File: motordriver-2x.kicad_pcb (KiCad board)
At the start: 4 copper layers, 215 x 130 mm, 651 parts, among them J1 USB_B_Micro, J2 CONN_RJ45_MAG, J3 CONN_RJ45_MAG, P1 CONN_BUTTON, P11 CONN_JOYSTICK, P13 CONN_SENSOR, P14 CONN_SENSOR, P15 CONN_SENSOR, P16 CONN_SENSOR, P17 CONN_DEBUG_2R, P18 CONN_POWER_41A, P19 CONN_CAN, P2 CONN_BUTTON, P20 CONN_CAN, P21 CONN_AN_OUT, P22 CONN_AN_OUT, P23 CONN_POWER_10A, P24 CONN_CAN, P25 CONN_LCD, P26 CONN_AN_OUT, P27 CONN_AN_OUT, P28 CONN_UEXT, P3 CONN_BUTTON, P37 CONN_ENCODER, P38 CONN_SENSOR, P39 CONN_SENSOR, P4 CONN_BUTTON, P40 CONN_SENSOR, P41 CONN_ENCODER, P42 CONN_SENSOR, P43 CONN_SENSOR, P44 CONN_SENSOR, P45 CONN_MOTOR, P46 CONN_MOTOR, P47 CONN_HALL, P48 CONN_HALL, P49 CONN_BRKRES, P5 CONN_BUTTON, P6 CONN_BUTTON, P7 CONN_BUTTON, P8 CONN_BUTTON, P9 CONN_JOYSTICK, Q1 Q_NMOS_2X_60V_63A, Q2 Q_NMOS_2X_60V_63A, Q3 Q_NMOS_2X_60V_63A, Q4 Q_NMOS_2X_60V_63A, Q5 Q_NMOS_2X_60V_63A, Q6 Q_NMOS_2X_60V_63A, Q7 Q_PNP_BC856, Q8 Q_NMOS_BUK9875, U1 IC_MIC2026, U10 IC_MCP4461, U11 IC_MCP2517FD-xJHA, U12 IC_STM32F429ZET6, U13 IC_MCP23S17, U14 IC_TPS54360DDA, U15 IC_TJA1044GT3, U16 IC_TLV2474, U17 IC_M24C16, U18 IC_USBLC6-2, U19 IC_TPS62147RGXR, U2 IC_MAX6818, U20 IC_TLV75533, U21 IC_LP55231, U22 IC_TLV75533, U23 IC_MAX14890, U24 IC_MAX14890, U25 IC_MIC2026, U26 IC_TLV2474, U27 IC_USBLC6-2, U28 IC_USBLC6-2, U29 IC_MCP4461, U3 IC_TLV2474, U30 IC_LAN9252, U31 IC_DRV8302, U32 IC_DRV8302, U33 IC_TLV2474, U34 IC_M24C16, U35 IC_TLV2474, U36 IC_TLV75533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

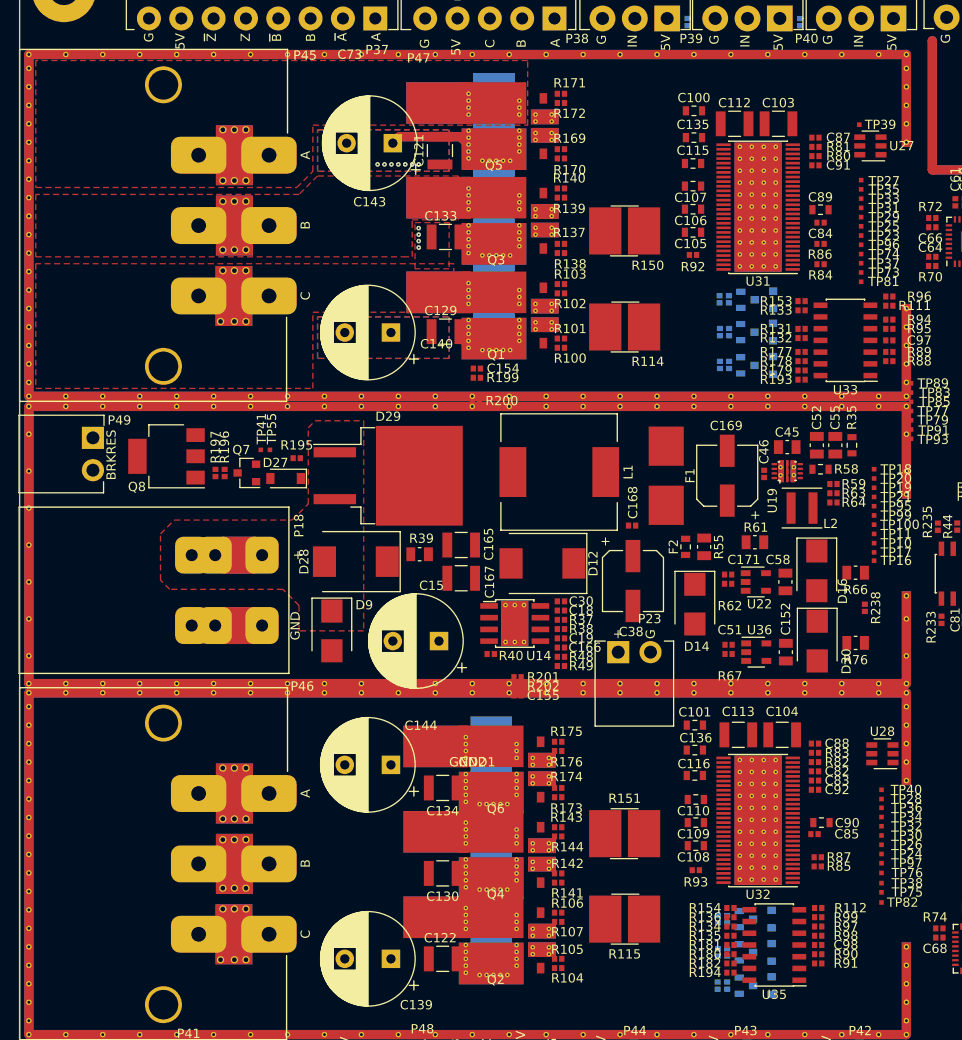
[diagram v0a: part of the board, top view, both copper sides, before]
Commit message: routing with fills
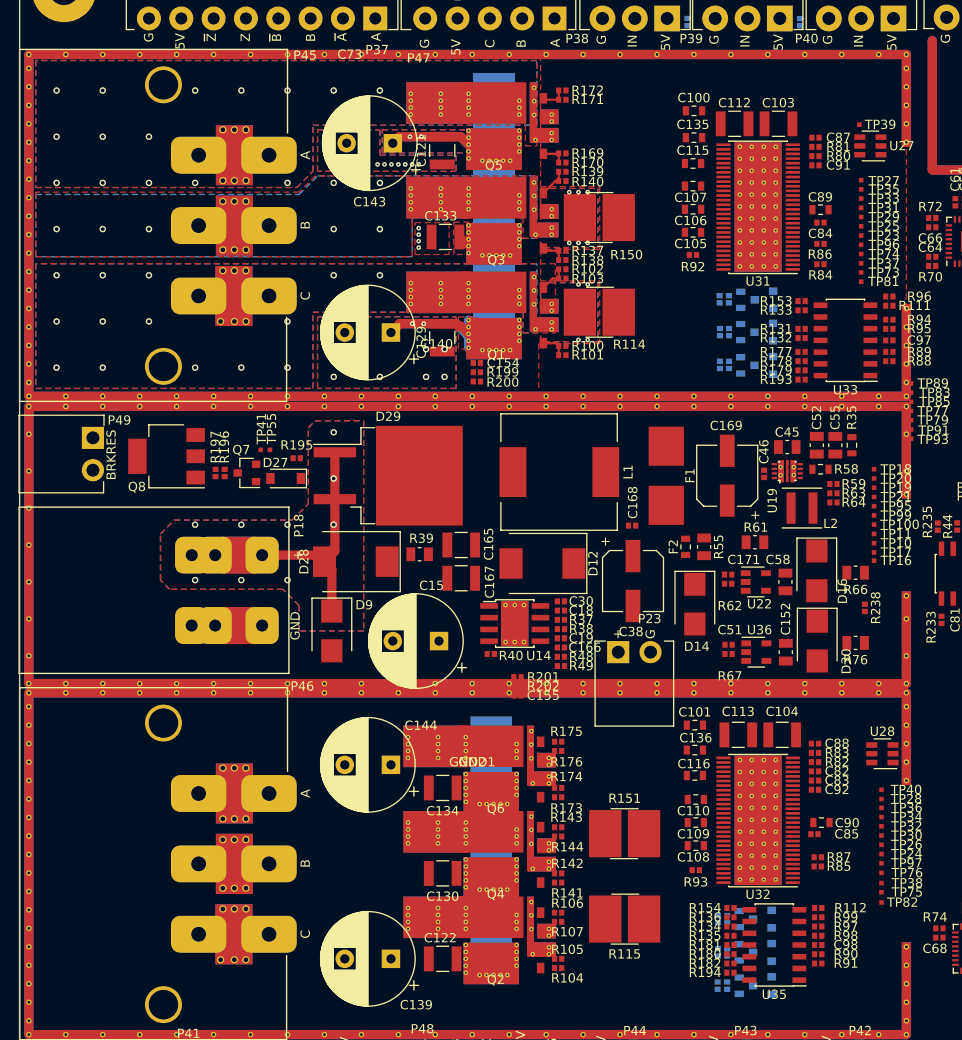
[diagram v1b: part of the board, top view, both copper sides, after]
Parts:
- moved R114 3.18 mm to (108.8, 64.0)
- moved R150 3.11 mm to (108.8, 53.8)
- moved R139 2.80 mm to (104.8, 48.8)
- moved R102 2.60 mm to (104.8, 59.4)
- moved R200 2.00 mm to (95.5, 71.5)
- moved R101 1.81 mm to (104.8, 68.7)
- moved R172 1.36 mm to (104.8, 40.0)
- moved R140 0.81 mm to (104.8, 49.8)
- moved R137 0.76 mm to (104.8, 57.4)
- moved R138 0.76 mm to (104.8, 58.4)
- moved C129 0.74 mm to (91.8, 66.8), turned to 270 degrees
- moved R171 0.67 mm to (104.8, 41.0)
- moved R103 0.62 mm to (104.8, 60.4)
- moved C154 0.60 mm to (95.5, 69.5)
- moved R199 0.60 mm to (95.5, 70.5)
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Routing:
- net VMOT: track 55.2 -> 121.3 mm, vias 0 -> 4
- net VMOT_IN: track 0.00 -> 25.0 mm, vias 0 -> 9
- net SLC1: track 0.00 -> 3.75 mm, vias 0 -> 15
- net Net-(Q3-Pad4): track 0.00 -> 3.20 mm
- net Net-(Q1-Pad4): track 0.00 -> 3.08 mm
- net Net-(Q1-Pad1): track 0.00 -> 2.79 mm
- net Net-(Q3-Pad1): track 0.00 -> 2.77 mm
- net Net-(Q5-Pad4): track 0.00 -> 2.72 mm
- net Net-(Q5-Pad1): track 0.00 -> 2.68 mm
- net SLB1: vias 0 -> 7
- net SLA1: vias 0 -> 14
- net Net-(C135-Pad1): vias 0 -> 6
- net Net-(C115-Pad1): vias 0 -> 4
- net GND: vias 11 -> 18
- added copper zone on B.Cu, net Net-(C115-Pad1)
- added copper zone on F.Cu, net Net-(C115-Pad1)
- added copper zone on B.Cu, net Net-(C135-Pad1)
- added copper zone on F.Cu, net Net-(C135-Pad1)
- added copper zone on B.Cu, net SLA1
- added copper zone on In2.Cu, net SLA1
- added copper zone on B.Cu, net SLB1
- added copper zone on In2.Cu, net SLB1
- added copper zone on B.Cu, net SLC1
- added copper zone on In2.Cu, net SLC1
- added copper zone on B.Cu, net VMOT
- added copper zone on F.Cu, net VMOT
- added copper zone on In2.Cu, net VMOT
- added copper zone on B.Cu, net VMOT_IN
- added copper zone on In2.Cu, net VMOT_IN

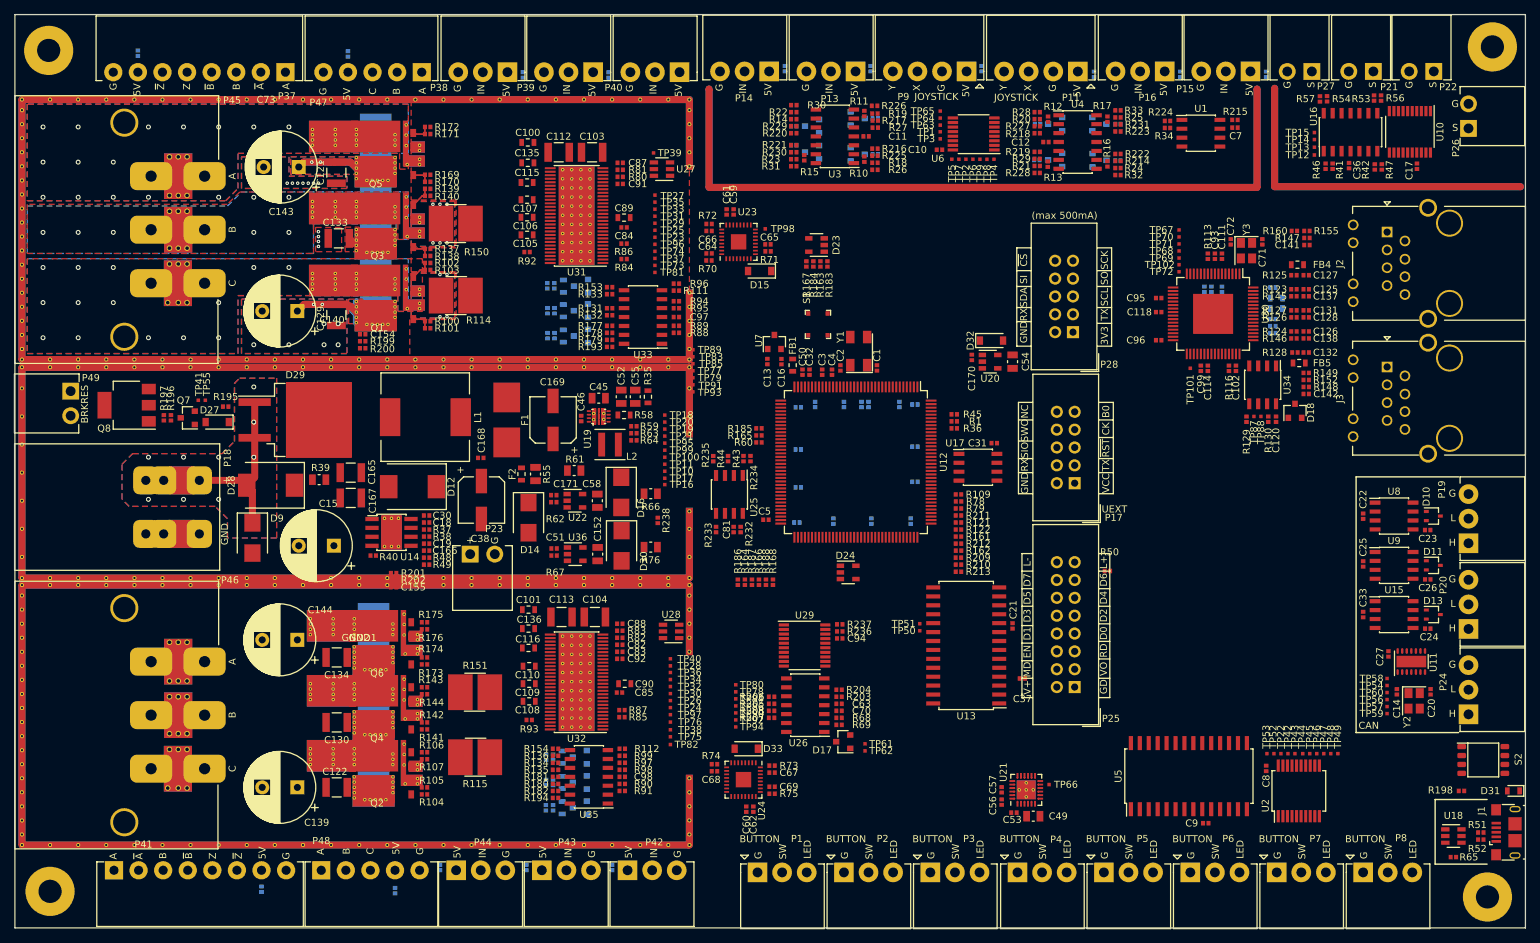
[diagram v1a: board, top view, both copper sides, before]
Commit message: fix many routing issues
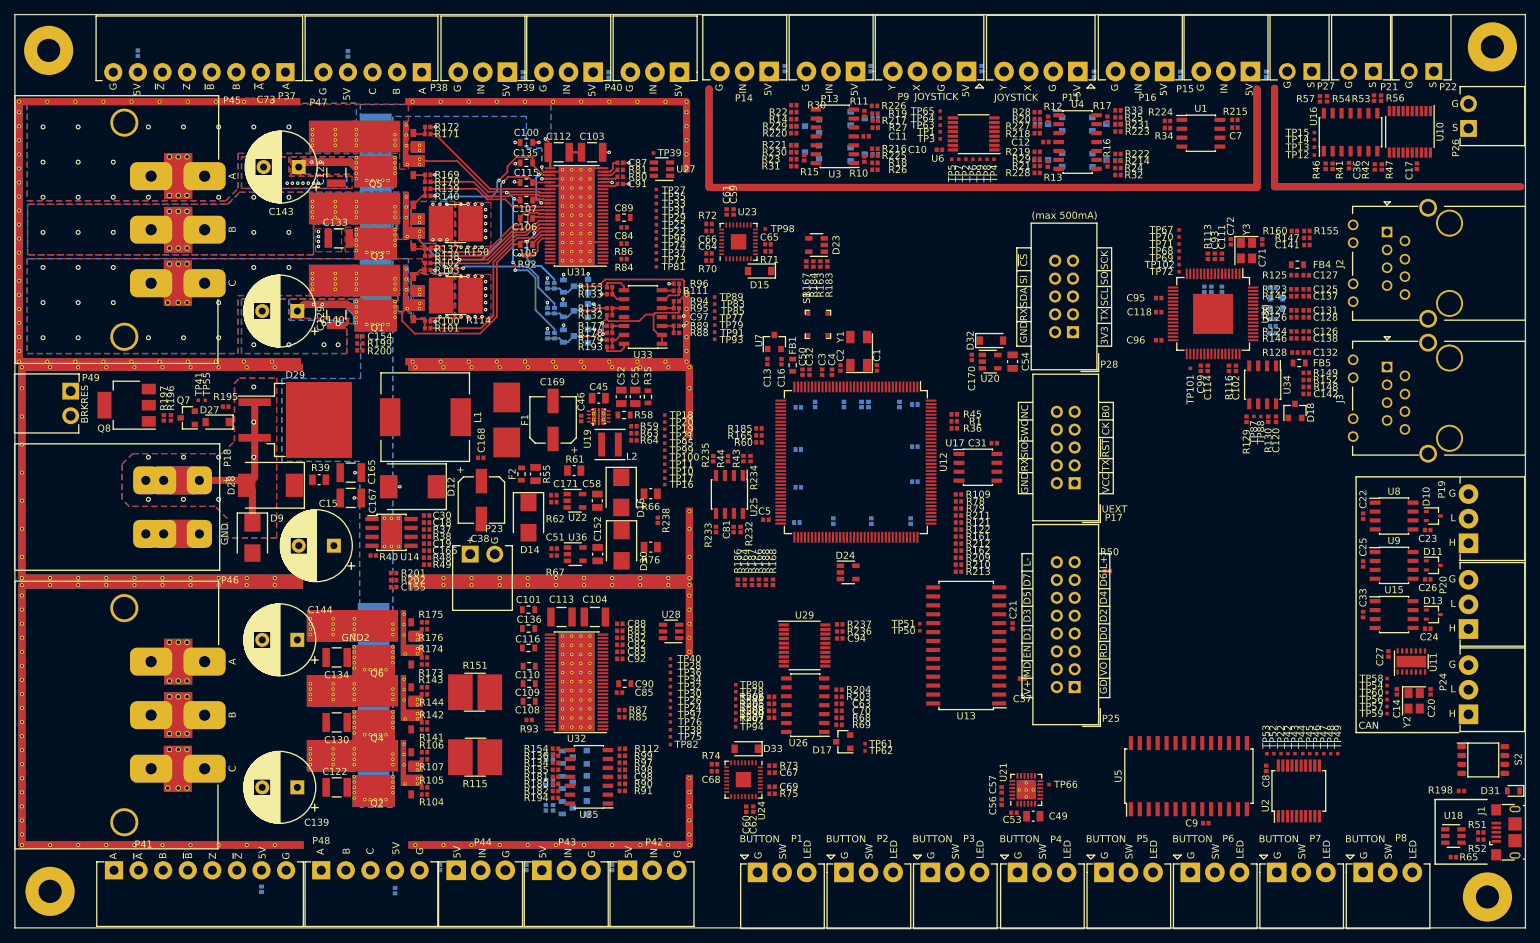
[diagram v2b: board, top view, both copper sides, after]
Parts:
- moved TP77 8.12 mm to (145.6, 67.2)
- moved TP79 8.12 mm to (145.6, 68.2)
- moved TP83 8.12 mm to (145.6, 65.2)
- moved TP85 8.12 mm to (145.6, 66.2)
- moved TP89 8.12 mm to (145.6, 64.2)
- moved TP91 8.12 mm to (145.6, 69.2)
- moved TP93 8.12 mm to (145.6, 70.2)
- moved C105 1.35 mm to (118.8, 56.7)
- moved TP23 0.82 mm to (137.3, 54.9)
- moved TP25 0.82 mm to (137.3, 53.9)
- moved TP27 0.82 mm to (137.3, 48.9)
- moved TP29 0.82 mm to (137.3, 52.9)
- moved TP31 0.82 mm to (137.3, 51.9)
- moved TP33 0.82 mm to (137.3, 50.9)
- moved TP35 0.82 mm to (137.3, 49.9)
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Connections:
- net GHA1 renamed GA1_P
- net GHB1 renamed GB1_P
- net GHC1 renamed GC1_P
- net GLA1 renamed GA1_N
- net GLB1 renamed GB1_N
- net GLC1 renamed GC1_N
- C105 pad 2: Net-(C105-Pad2) -> SHA1
- C106 pad 2: Net-(C106-Pad2) -> SHB1
- C107 pad 2: Net-(C107-Pad2) -> SHC1
- C108 pad 2: Net-(C108-Pad2) -> SHA2
- C109 pad 2: Net-(C109-Pad2) -> SHB2
- C110 pad 2: Net-(C110-Pad2) -> SHC2
- C115 pad 1: Net-(C115-Pad1) -> SLA1
- C116 pad 1: Net-(C116-Pad1) -> SLA2
- C135 pad 1: Net-(C135-Pad1) -> SLB1
- C136 pad 1: Net-(C136-Pad1) -> SLB2
- P45 pad 1: SLC1 -> SHC1
- P45 pad 2: SLB1 -> SHB1
- P45 pad 3: SLA1 -> SHA1
- P46 pad 1: SLC2 -> SHC2
- P46 pad 2: SLB2 -> SHB2
- P46 pad 3: SLA2 -> SHA2
- Q1 pad 2: SLA1 -> SHA1
- Q1 pad 3: Net-(C115-Pad1) -> SLA1
- Q1 pad 5: SLA1 -> SHA1
- Q2 pad 2: SLA2 -> SHA2
- Q2 pad 3: Net-(C116-Pad1) -> SLA2
- Q2 pad 5: SLA2 -> SHA2
- Q3 pad 2: SLB1 -> SHB1
- Q3 pad 3: Net-(C135-Pad1) -> SLB1
- Q3 pad 5: SLB1 -> SHB1
- Q4 pad 2: SLB2 -> SHB2
- Q4 pad 3: Net-(C136-Pad1) -> SLB2
- Q4 pad 5: SLB2 -> SHB2
- Q5 pad 2: SLC1 -> SHC1
- Q5 pad 5: SLC1 -> SHC1
- Q6 pad 2: SLC2 -> SHC2
- Q6 pad 5: SLC2 -> SHC2
- R114 pad 2: Net-(C115-Pad1) -> SLA1
- R115 pad 2: Net-(C116-Pad1) -> SLA2
- R117 pad 1: SLA1 -> SHA1
- R119 pad 1: SLA2 -> SHA2
- R150 pad 1: Net-(C135-Pad1) -> SLB1
- R151 pad 1: Net-(C136-Pad1) -> SLB2
- R156 pad 1: SLB1 -> SHB1
- R158 pad 1: SLB2 -> SHB2
- R189 pad 1: SLC1 -> SHC1
- R191 pad 1: SLC2 -> SHC2
- U31 pad 31: Net-(C135-Pad1) -> SLB1
- U31 pad 33: Net-(C115-Pad1) -> SLA1
- U31 pad 34: SLC1 -> GND
- U31 pad 36: Net-(C107-Pad2) -> SHC1
- U31 pad 41: Net-(C106-Pad2) -> SHB1
- U31 pad 46: Net-(C105-Pad2) -> SHA1
- U32 pad 31: Net-(C136-Pad1) -> SLB2
- U32 pad 33: Net-(C116-Pad1) -> SLA2
- U32 pad 34: SLC2 -> GND
- U32 pad 36: Net-(C110-Pad2) -> SHC2
- U32 pad 41: Net-(C109-Pad2) -> SHB2
- U32 pad 46: Net-(C108-Pad2) -> SHA2
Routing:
- net SHC1: track 0.00 -> 50.2 mm, vias 0 -> 19
- net SHB1: track 0.00 -> 49.0 mm, vias 0 -> 9
- net SHA1: track 0.00 -> 43.8 mm, vias 0 -> 16
- net SLA1: track 0.00 -> 40.9 mm, vias 14 -> 6
- net GND: track 0.00 -> 36.4 mm, vias 18 -> 76
- net GA1_P: track 0.00 -> 27.3 mm
- net SLB1: track 0.00 -> 27.2 mm, vias 7 -> 9
- net VSA1_RAW: track 0.00 -> 23.8 mm, vias 0 -> 1
- net GB1_P: track 0.00 -> 20.4 mm
- net GC1_N: track 0.00 -> 20.3 mm
- net Net-(R132-Pad1): track 0.00 -> 20.2 mm, vias 0 -> 2
- net GA1_N: track 0.00 -> 19.4 mm
- net GC1_P: track 0.00 -> 19.1 mm
- net GB1_N: track 0.00 -> 18.2 mm
- net VSC1_RAW: track 0.00 -> 9.68 mm, vias 0 -> 1
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- added copper zone on F.Cu, net (none)
- added copper zone on B.Cu, net SHA1
- added copper zone on F.Cu, net SHA1
- added copper zone on In2.Cu, net SHA1
- added copper zone on B.Cu, net SHB1
- added copper zone on F.Cu, net SHB1
- added copper zone on In2.Cu, net SHB1
- added copper zone on B.Cu, net SHC1
- added copper zone on F.Cu, net SHC1
- added copper zone on In2.Cu, net SHC1
- removed copper zone on B.Cu, net Net-(C115-Pad1)
- removed copper zone on F.Cu, net Net-(C115-Pad1)
- removed copper zone on B.Cu, net Net-(C135-Pad1)
- removed copper zone on F.Cu, net Net-(C135-Pad1)
- removed copper zone on In2.Cu, net SLA1
- removed copper zone on In2.Cu, net SLB1
- removed copper zone on B.Cu, net SLC1
- removed copper zone on F.Cu, net SLC1
- removed copper zone on In2.Cu, net SLC1

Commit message: routing power supply
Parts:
- moved R39 9.92 mm to (96.8, 96.8)
- moved C168 8.03 mm to (119.2, 91.1), turned to 270 degrees
- moved TP95 7.95 mm to (141.8, 92.2)
- moved TP100 7.04 mm to (141.8, 93.2)
- moved D28 5.36 mm to (87.8, 90.8)
- moved R61 4.66 mm to (130.2, 89.2)
- moved P23 4.06 mm to (114.8, 101.8)
- moved R55 3.46 mm to (123.5, 88.8)
- moved C165 3.25 mm to (97.0, 89.8), turned to 180 degrees
- moved C167 3.23 mm to (97.0, 93.2), turned to 180 degrees
- moved F2 3.22 mm to (121.2, 88.8)
- moved C166 3.01 mm to (107.6, 100.0)
- moved C18 3.01 mm to (107.6, 96.0)
- moved C19 3.01 mm to (107.6, 99.0)
- moved R37 3.01 mm to (107.6, 97.0)
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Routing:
- net VMOT: track 127.7 -> 20.4 mm, vias 6 -> 46
- net GND: track 36.4 -> 72.2 mm, vias 76 -> 97
- net Net-(C168-Pad1): track 0.00 -> 34.1 mm
- net Net-(C169-Pad1): track 0.00 -> 22.6 mm
- net Net-(C30-Pad1): track 0.00 -> 20.6 mm
- net Net-(R35-Pad2): track 0.00 -> 10.9 mm
- net Net-(C58-Pad1): track 0.00 -> 10.7 mm
- net Net-(Q8-Pad1): track 0.00 -> 10.7 mm
- net Net-(C152-Pad1): track 0.00 -> 10.7 mm
- net Net-(D27-Pad2): track 0.00 -> 7.85 mm
- net Net-(D14-Pad1): track 0.00 -> 6.21 mm
- net Net-(R58-Pad2): track 0.00 -> 6.05 mm, vias 0 -> 2
- net Net-(C30-Pad2): track 0.00 -> 6.05 mm
- net USB_5V: track 0.00 -> 5.15 mm
- net Net-(Q7-Pad3): track 0.00 -> 4.38 mm
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- added copper zone on F.Cu, net Net-(P49-Pad2)
